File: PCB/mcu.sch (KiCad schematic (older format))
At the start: 59 parts, among them P1 USB_CONN, P11 2PIN, P12 2PIN, P13 2PIN, P15 2PIN, P2 USB3, P3 USB3_MICRO, P4 6PIN, P5 6PIN, P6 ISP6, P7_1 5PIN, P7_2 5PIN, U1 Atmega32u4, U2 MCP23018, U3 IP4234CZ6, U4 74HC138, U5 PAM2804, X1 CRYSTAL

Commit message: Rev 0.7
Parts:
- removed R36: 1k, prettylib:SMD_0805, symbol R
- JP1: footprint prettylib:JUMPER_SMD_2 -> prettylib:JUMPER_SMD_3; symbol JUMPER -> JUMPER3
- R9: value 100k -> 10k; Description RES SMD 100K OHM 1% 1/8W 0805 -> RES SMD 10K OHM 1% 1/8W 0805; Product RC2012F104CS -> RC2012F103CS; URL http://www.digikey.com/product-detail/en/samsung-electro-me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 -> (none)
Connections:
- wire segments 147 -> 149
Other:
- moved on the sheet: R9
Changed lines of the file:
@@
 Sheet 3 3
 Title "TS65"
-Date "2016-05-01"
-Rev "Rev 0.6"
+Date "2016-05-17"
+Rev "Rev 0.7"
 Comp "MOZ"
 Comment1 ""
@@
 XTAL2
 $Comp
-L JUMPER JP1
+L JUMPER3 JP1
 U 1 1 56F1A7A6
-P 5450 7000
-F 0 "JP1" H 5450 7150 60  0000 C CNN
-F 1 "JUMPER" H 5450 6920 40  0000 C CNN
-F 2 "prettylib:JUMPER_SMD_2" H 5450 7000 60  0001 C CNN
-F 3 "" H 5450 7000 60  0000 C CNN
-F 4 "Jumper to pull down HWBE" H 5450 7000 60  0001 C CNN "Description"
-	1    5450 7000
-	-1   0    0    -1
+P 4700 6800
+F 0 "JP1" H 4700 6950 60  0000 C CNN
+F 1 "JUMPER" H 4850 6700 40  0000 C CNN
+F 2 "prettylib:JUMPER_SMD_3" H 4700 6800 60  0001 C CNN
+F 3 "" H 4700 6800 60  0000 C CNN
+F 4 "Jumper to pull down HWBE" H 4700 6800 60  0001 C CNN "Description"
+	1    4700 6800
+	1    0    0    1
 $EndComp
 $Comp
 L VSS #PWR022
 U 1 1 56F1BFE6
-P 6300 7050
-F 0 "#PWR022" H 6300 7050 30  0001 C CNN
-F 1 "VSS" H 6300 6980 30  0000 C CNN
-F 2 "" H 6300 7050 60  0000 C CNN
-F 3 "" H 6300 7050 60  0000 C CNN
-	1    6300 7050
+P 5000 6850
+F 0 "#PWR022" H 5000 6850 30  0001 C CNN
+F 1 "VSS" H 5000 6780 30  0000 C CNN
+F 2 "" H 5000 6850 60  0000 C CNN
+F 3 "" H 5000 6850 60  0000 C CNN
+	1    5000 6850
 	-1   0    0    -1
 $EndComp
-Text Notes 5700 6900 0    59   ~ 0
+Text Notes 4450 7100 0    59   ~ 0
 HWBE Jumper
 Text Notes 8150 6700 0    59   ~ 0
@@
 L R R9
 U 1 1 56E18C9E
-P 4900 7000
-F 0 "R9" V 4980 7000 40  0000 C CNN
-F 1 "100k" V 4907 7001 40  0000 C CNN
-F 2 "prettylib:SMD_0805" V 4830 7000 30  0001 C CNN
-F 3 "" H 4900 7000 30  0000 C CNN
-F 4 "RES SMD 100K OHM 1% 1/8W 0805" V 4900 7000 60  0001 C CNN "Description"
-F 5 "RC2012F104CS" V 4900 7000 60  0001 C CNN "Product"
-F 6 "http://www.digikey.com/product-detail/en/samsung-electro-mechanics-america-inc/RC2012F104CS/1276-3512-1-ND/3903615" V 4900 7000 60  0001 C CNN "URL"
-F 7 "Samsung" V 4900 7000 60  0001 C CNN "Vendor"
-	1    4900 7000
-	0    1    -1   0
+P 5000 6300
+F 0 "R9" V 5080 6300 40  0000 C CNN
+F 1 "10k" V 5007 6301 40  0000 C CNN
+F 2 "prettylib:SMD_0805" V 4930 6300 30  0001 C CNN
+F 3 "" H 5000 6300 30  0000 C CNN
+F 4 "RES SMD 10K OHM 1% 1/8W 0805" V 5000 6300 60  0001 C CNN "Description"
+F 5 "RC2012F103CS" V 5000 6300 60  0001 C CNN "Product"
+F 6 "~" V 5000 6300 60  0001 C CNN "URL"
+F 7 "Samsung" V 5000 6300 60  0001 C CNN "Vendor"
+	1    5000 6300
+	0    -1   1    0
 $EndComp
 $Comp
@@
 	1    1750 9050
 	1    0    0    -1
-$EndComp
-$Comp
-L R R36
-U 1 1 56FBC6EE
-P 6000 7000
-F 0 "R36" V 6080 7000 40  0000 C CNN
-F 1 "1k" V 6007 7001 40  0000 C CNN
-F 2 "prettylib:SMD_0805" V 5930 7000 30  0001 C CNN
-F 3 "" H 6000 7000 30  0000 C CNN
-F 4 "RES SMD 1K OHM 1% 1/8W 0805" V 6000 7000 60  0001 C CNN "Description"
-F 5 "RC2012F102CS" V 6000 7000 60  0001 C CNN "Product"
-F 6 "http://www.digikey.com/product-detail/en/samsung-electro-mechanics-america-inc/RC2012F102CS/1276-5272-1-ND/3968244" V 6000 7000 60  0001 C CNN "URL"
-F 7 "Samsung" V 6000 7000 60  0001 C CNN "Vendor"
-	1    6000 7000
-	0    1    1    0
 $EndComp
 $Comp
@@
 L +5V #PWR036
 U 1 1 571EF3AD
-P 4650 7000
-F 0 "#PWR036" H 4650 7090 20  0001 C CNN
-F 1 "+5V" H 4650 7090 30  0000 C CNN
-F 2 "" H 4650 7000 60  0000 C CNN
-F 3 "" H 4650 7000 60  0000 C CNN
-	1    4650 7000
+P 4400 6750
+F 0 "#PWR036" H 4400 6840 20  0001 C CNN
+F 1 "+5V" H 4400 6840 30  0000 C CNN
+F 2 "" H 4400 6750 60  0000 C CNN
+F 3 "" H 4400 6750 60  0000 C CNN
+	1    4400 6750
 	1    0    0    -1
 $EndComp
@@
 Wire Notes Line
 	13150 9750 15800 9750
-Wire Wire Line
-	4850 6850 5150 6850
-Wire Wire Line
-	4850 6300 4850 6850
-Wire Wire Line
-	5450 6300 4850 6300
 Wire Notes Line
 	750  10900 3700 10900
@@
 Wire Wire Line
 	1300 9600 2650 9600
-Wire Wire Line
-	5150 6850 5150 7000
 Wire Notes Line
 	750  7700 3700 7700
@@
 	8800 1400 4100 1400
 Wire Wire Line
-	6300 7000 6300 7050
-Wire Wire Line
-	6250 7000 6300 7000
+	5000 6650 5000 6850
+Wire Wire Line
+	4950 6800 5000 6800
 Wire Notes Line
 	12950 9750 11000 9750
@@
 Wire Wire Line
 	5300 3800 5450 3800
+Wire Wire Line
+	4400 6750 4400 6800
+Wire Wire Line
+	4400 6800 4450 6800
+Wire Wire Line
+	4700 6700 4700 6300
+Wire Wire Line
+	4700 6300 4750 6300
+Wire Wire Line
+	5000 6650 4700 6650
+Connection ~ 4700 6650
+Connection ~ 5000 6800
+Wire Wire Line
+	5250 6300 5450 6300
 $EndSCHEMATC

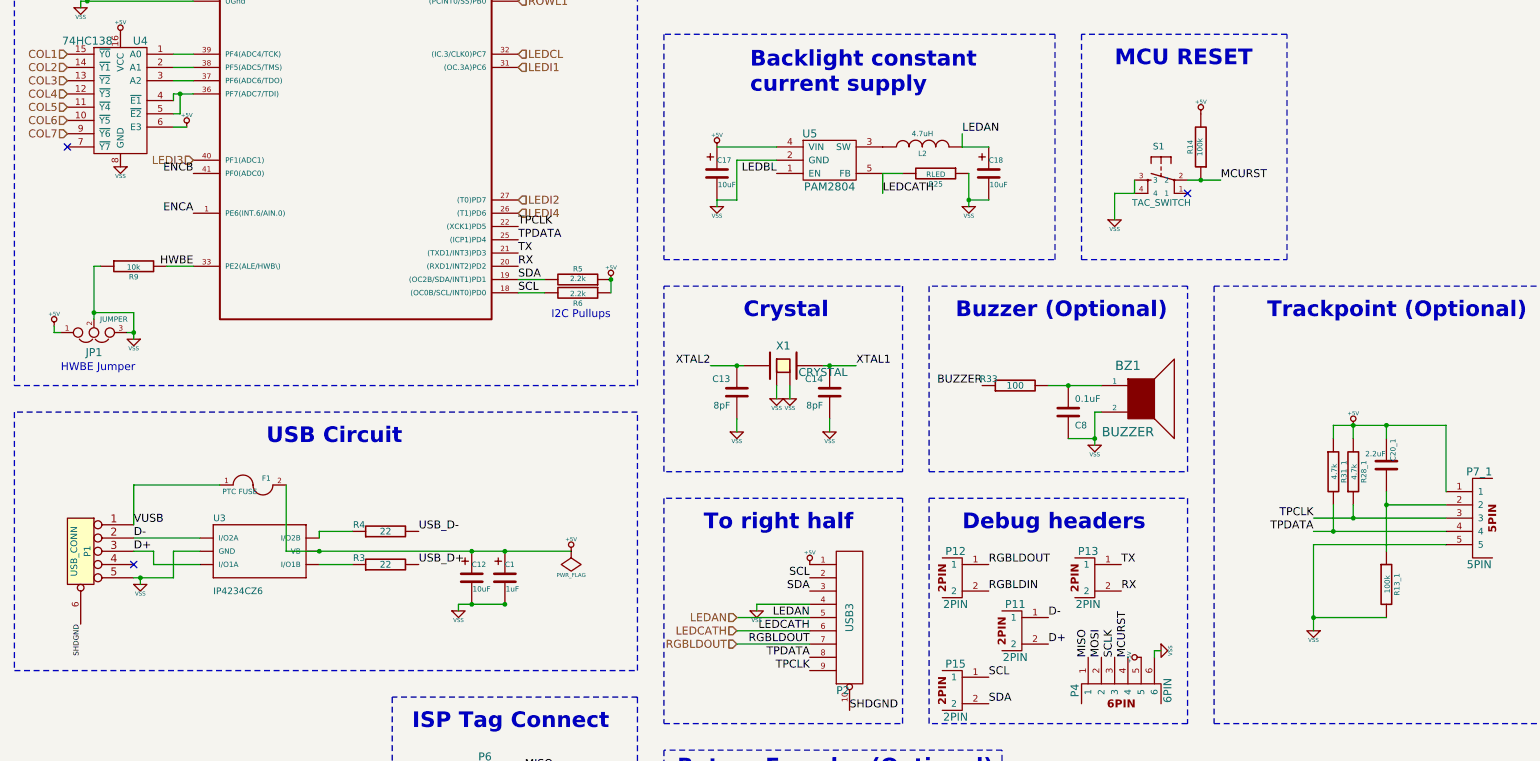
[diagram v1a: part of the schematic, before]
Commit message: 0.7.1
- Corrected pin mappings for right half connector
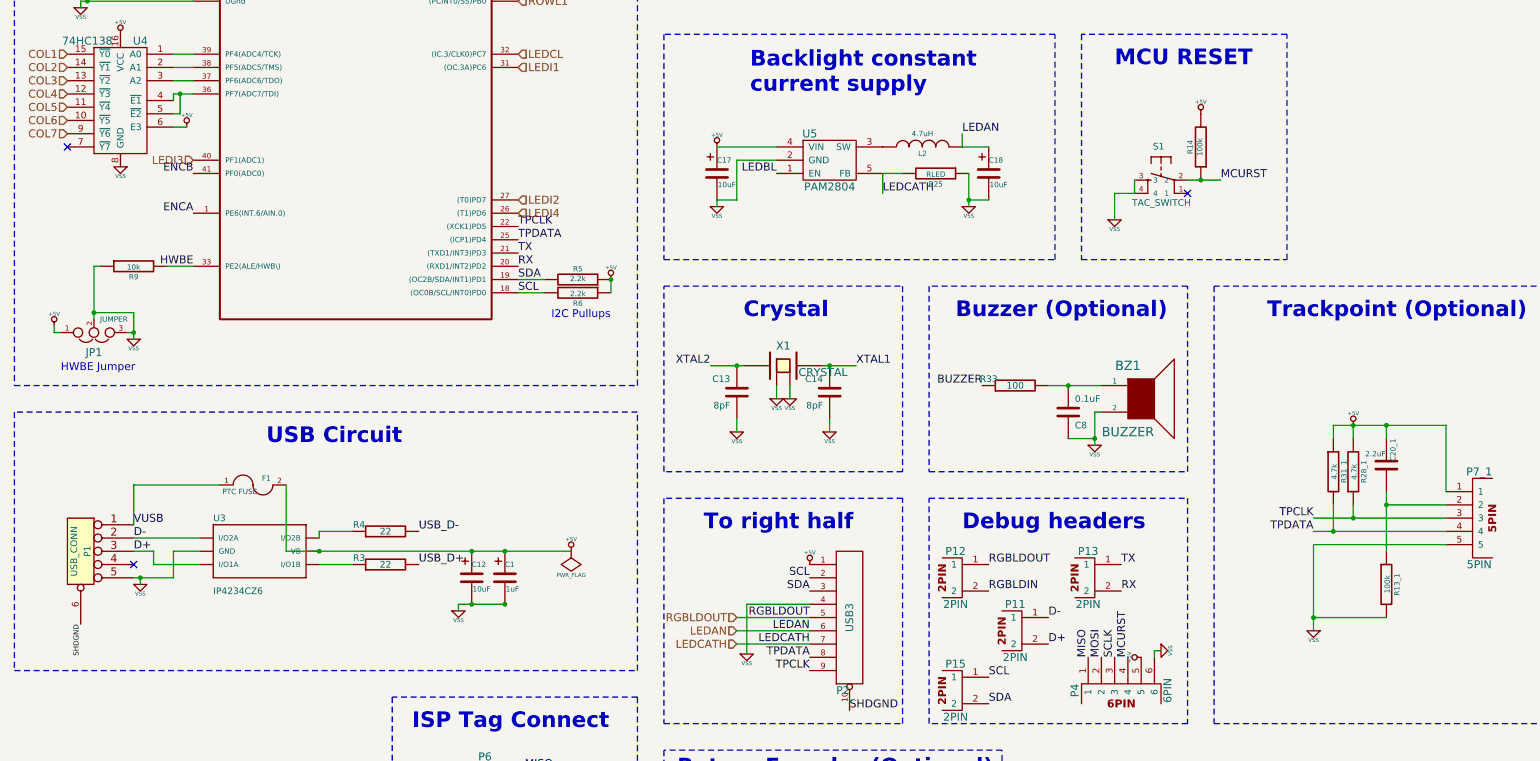
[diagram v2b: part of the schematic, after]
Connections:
- net LEDAN: now also P2.6; no longer P2.5
- net LEDCATH: now also P2.7; no longer P2.6
- net RGBLDOUT: now also P2.5; no longer P2.7
